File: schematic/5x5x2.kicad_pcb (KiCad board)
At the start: 4 copper layers, 204 x 100 mm, 186 parts, among them J1 SW Debug, J10 Conn_01x03_Female, J11 Conn_01x03_Male, J12 Conn_01x03_Male, J13 Conn_01x03_Female, J14 Conn_01x03_Female, J15 Conn_01x03_Male, J16 Conn_01x03_Female, J2 USB_C_Receptacle_USB2.0, J3 Conn_01x03_Male, J4 Conn_01x03_Male, J5 Conn_01x03_Female, J6 Conn_01x03_Female, J7 Conn_01x03_Male, J8 Conn_01x03_Male, J9 Conn_01x03_Female, SW1 SW, SW11 SW, SW12 SW, SW13 SW, SW14 SW, SW15 SW, SW21 SW, SW22 SW, SW23 SW, SW24 SW, SW25 SW, SW31 SW, SW32 SW, SW33 SW, SW34 SW, SW35 SW, SW41 SW, SW42 SW, SW43 SW, SW44 SW, SW45 SW, SW51 SW, SW52 SW, SW53 SW, SW54 SW, SW55 SW, SW6 ALPS_EC11, U1 SRV0504, U2 STM32F103C8, U3 LD1117S33CTR, Y1 16M

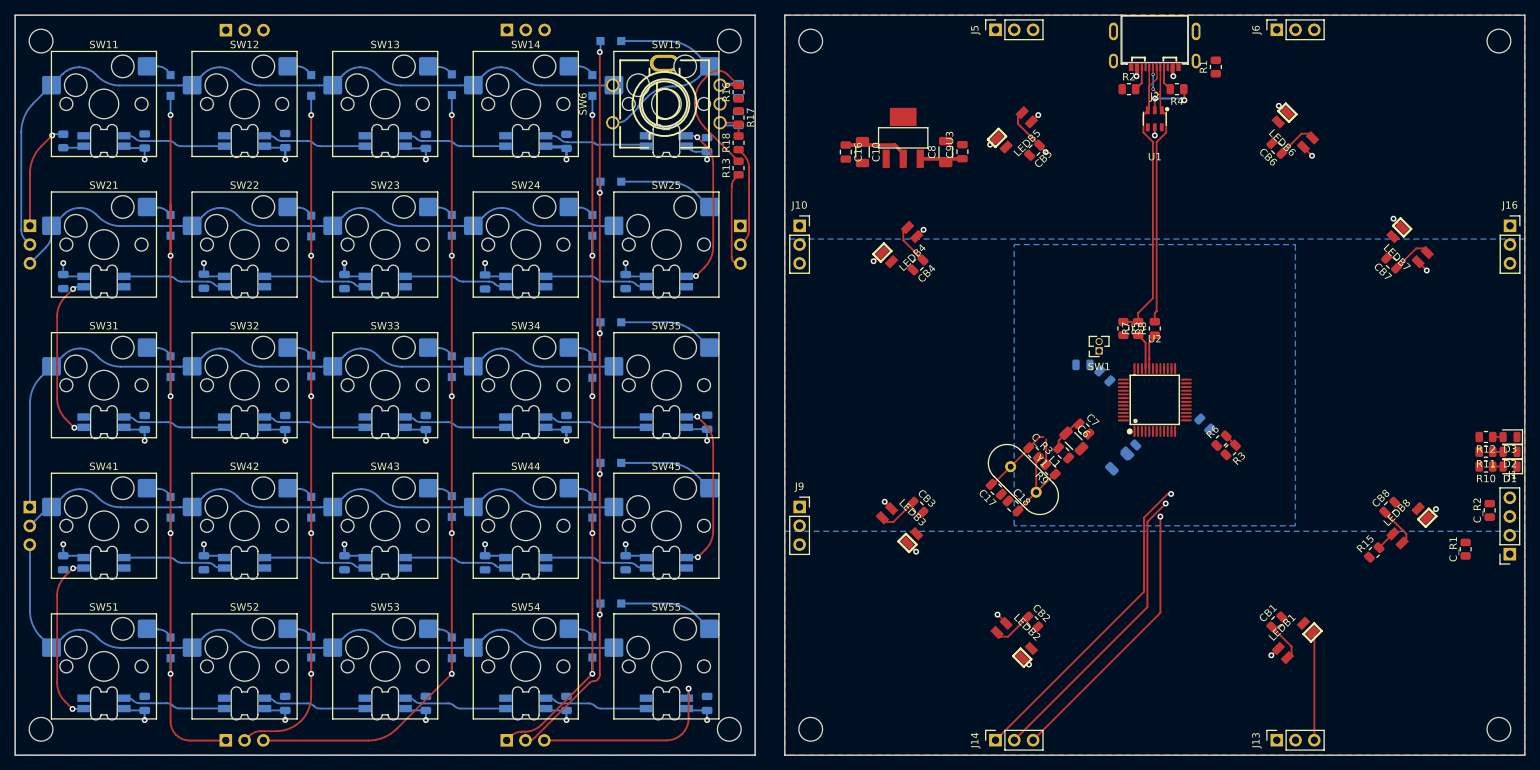
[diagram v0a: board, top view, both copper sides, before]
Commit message: Routed all remaining parts.
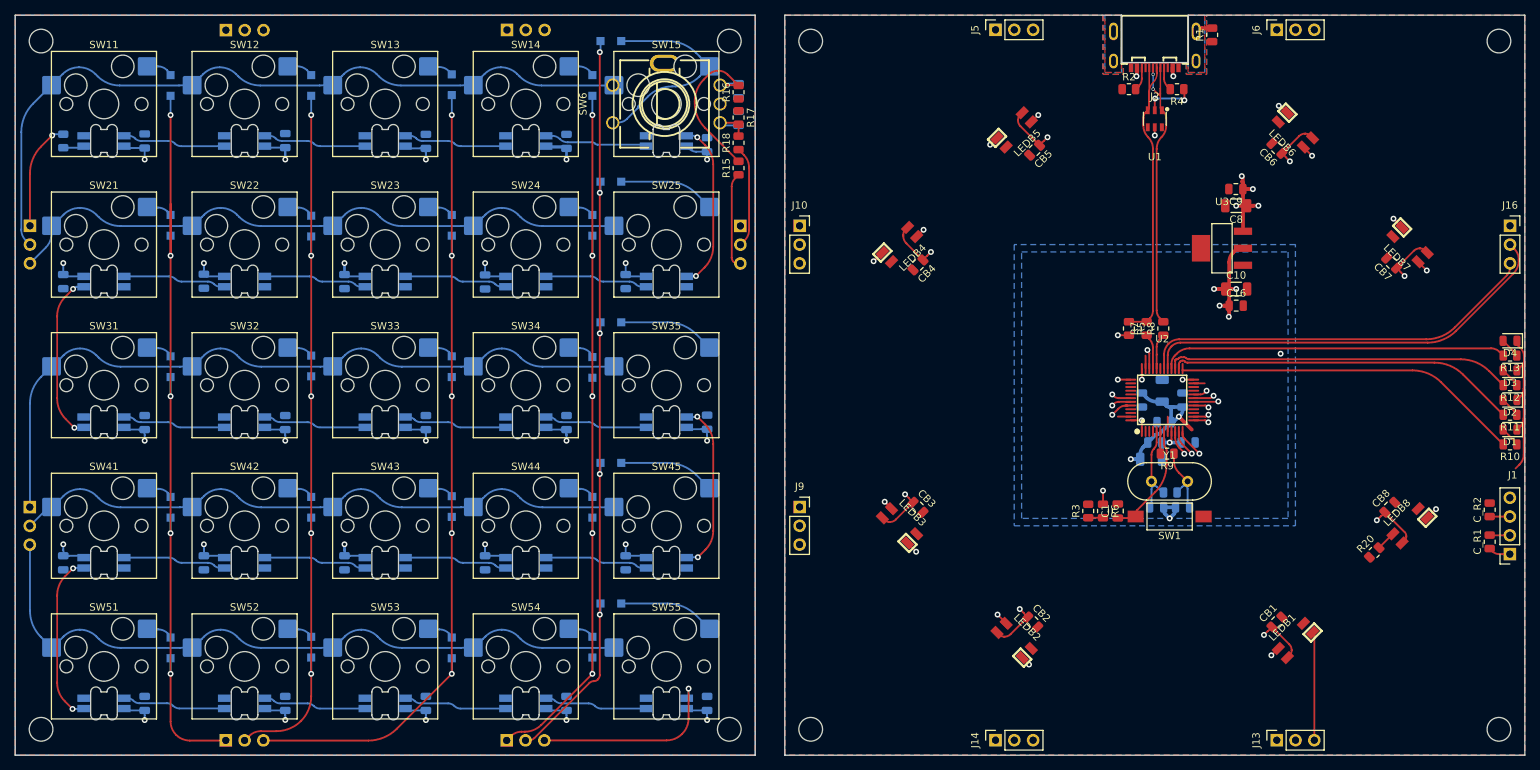
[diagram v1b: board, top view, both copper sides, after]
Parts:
- added D4: Led_Small, LED_SMD:LED_0805_2012Metric, F.Cu at (238.0, 82.0)
- added R13: 1k, Resistor_SMD:R_0805_2012Metric, F.Cu at (238.0, 84.0)
- C1: moved to F.Cu
- C17, C18, C6, C7, C_R3, L1: moved to B.Cu
- SW1: footprint Connector_PinSocket_1.27mm:PinSocket_1x02_P1.27mm_Vertical -> Button_Switch_SMD:SW_SPST_FSMSM
- moved C16 56.7 mm to (201.0, 77.2), turned to 0 degrees
- moved C10 53.8 mm to (201.0, 75.0), turned to 0 degrees
- moved U3 45.6 mm to (199.1, 69.5), turned to 0 degrees
- moved C8 39.9 mm to (201.0, 63.8), turned to 180 degrees
- moved C9 37.3 mm to (200.9, 61.5), turned to 180 degrees
- moved SW1 24.3 mm to (192.0, 105.8)
- moved C18 22.9 mm to (193.8, 104.5), turned to 0 degrees
- moved C17 21.8 mm to (190.2, 104.5), turned to 180 degrees
- moved R3 20.9 mm to (181.0, 105.0), turned to 90 degrees
- moved C1 20.3 mm to (185.0, 105.0), turned to 90 degrees
- moved C_R3 19.3 mm to (192.1, 102.5), turned to 0 degrees
- moved Y1 19.1 mm to (189.6, 101.0), turned to 0 degrees
- moved R6 18.6 mm to (183.0, 105.0), turned to -90 degrees
- moved L1 16.9 mm to (194.5, 95.8), turned to 180 degrees
- moved R9 15.9 mm to (191.7, 97.2), turned to 180 degrees
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- renumbered R13 to R15, R14 to R19, R15 to R20
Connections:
- net /USBD+ renamed Net-(R7-Pad1)
- net /USBD- renamed Net-(R8-Pad1)
- net Net-(C1-Pad1) renamed /~RESET
- net Net-(J2-PadS1) renamed /SHIELD
- U2 pad 2: Net-(R10-Pad2) -> unconnected-(U2-Pad2)
- U2 pad 25: unconnected-(U2-Pad25) -> Net-(R10-Pad2)
- U2 pad 26: unconnected-(U2-Pad26) -> Net-(R11-Pad2)
- U2 pad 27: unconnected-(U2-Pad27) -> Net-(R12-Pad2)
- U2 pad 28: unconnected-(U2-Pad28) -> Net-(U2-Pad28)
- U2 pad 3: Net-(R11-Pad2) -> unconnected-(U2-Pad3)
- U2 pad 4: Net-(R12-Pad2) -> unconnected-(U2-Pad4)
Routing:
- net COL4: track 102.7 -> 179.7 mm, vias 5 -> 6
- net BACKLIGHTIN: track 14.8 -> 88.6 mm, vias 1 -> 2
- net ROW5: track 96.4 -> 166.8 mm, vias 0 -> 1
- net ROTD: track 104.9 -> 175.0 mm, vias 0 -> 1
- net COL5: track 105.6 -> 175.4 mm, vias 5 -> 6
- net Net-(C_R2-Pad1): track 0.00 -> 69.0 mm, vias 0 -> 1
- net ROW2: track 87.7 -> 155.2 mm, vias 0 -> 1
- net ROW4: track 85.5 -> 152.2 mm, vias 0 -> 1
- net Net-(C_R1-Pad2): track 0.00 -> 64.6 mm, vias 0 -> 1
- net ROW3: track 101.5 -> 161.8 mm, vias 0 -> 1
- net +3V3: track 8.96 -> 67.7 mm, vias 0 -> 9
- net GND: track 7.20 -> 65.0 mm, vias 2 -> 5
- net ROTA: track 13.7 -> 71.3 mm
- net ROTB: track 13.1 -> 67.5 mm
- net Net-(R11-Pad2): track 0.00 -> 47.4 mm
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- added copper zone on B.Cu, net /SHIELD
- added copper zone on F.Cu, net /SHIELD

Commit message: Cleaned up silkscreen.
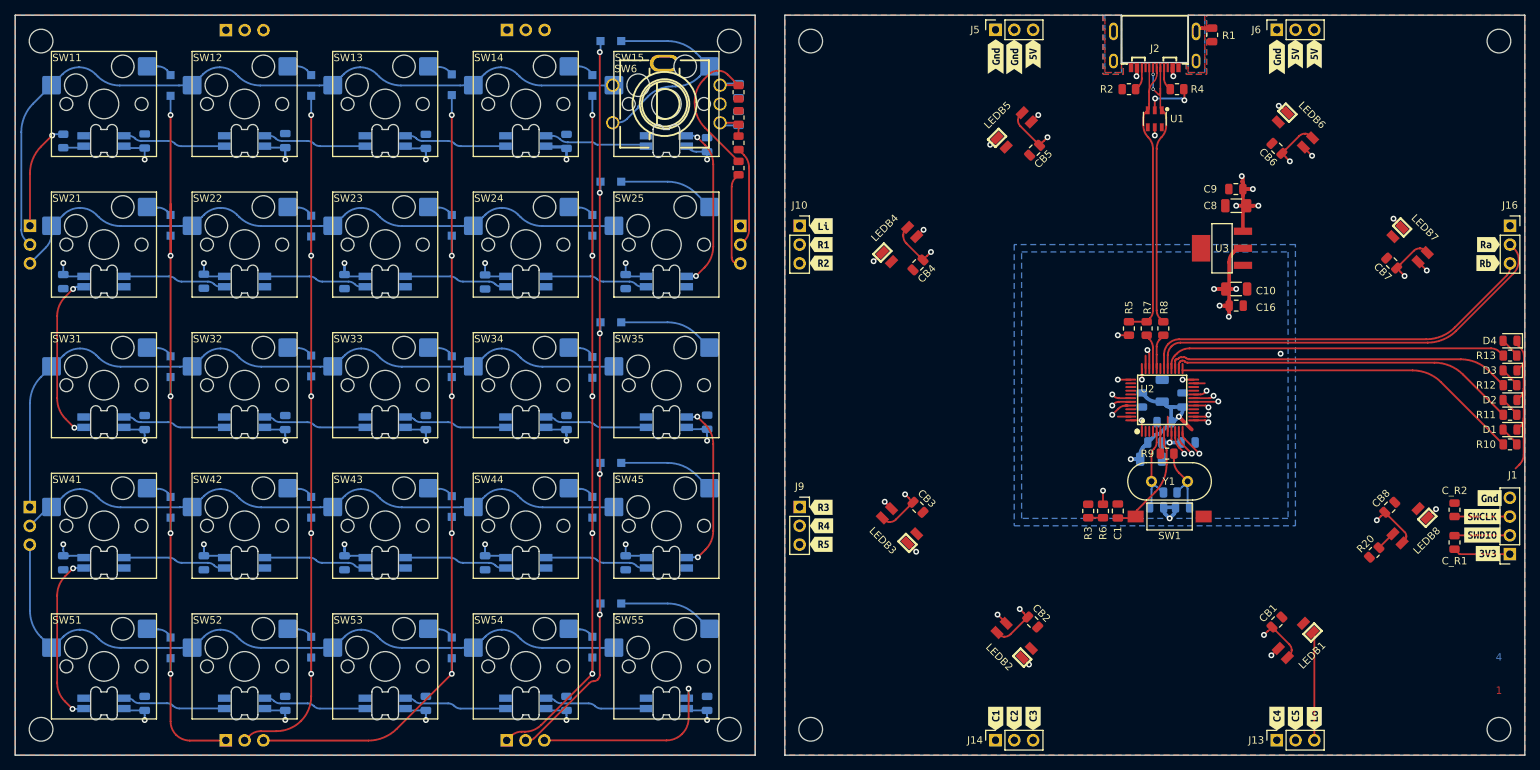
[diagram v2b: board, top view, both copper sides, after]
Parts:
- added G***: LOGO, LOGO, B.Cu at (131.2, 112.8)
- added G***: LOGO, LOGO, B.Cu at (190.0, 133.8)
- added kibuzzard-62AF6B0E: G***, kibuzzard-62AF6B0E, B.Cu at (38.0, 102.0)
- added kibuzzard-62AF6B38: G***, kibuzzard-62AF6B38, B.Cu at (40.5, 107.0)
- added kibuzzard-62AF6B38: G***, kibuzzard-62AF6B38, B.Cu at (145.0, 107.0)
- added kibuzzard-62AF6B7C: G***, kibuzzard-62AF6B7C, B.Cu at (145.0, 109.5)
- added kibuzzard-62AF6B7C: G***, kibuzzard-62AF6B7C, B.Cu at (40.5, 109.5)
- added kibuzzard-62AF6BA3: G***, kibuzzard-62AF6BA3, B.Cu at (145.0, 71.5)
- added kibuzzard-62AF6BA3: G***, kibuzzard-62AF6BA3, B.Cu at (40.5, 71.5)
- added kibuzzard-62AF6BAD: G***, kibuzzard-62AF6BAD, B.Cu at (40.5, 69.0)
- added kibuzzard-62AF6BAD: G***, kibuzzard-62AF6BAD, B.Cu at (145.0, 69.0)
- added kibuzzard-62AF6BF3: G***, kibuzzard-62AF6BF3, B.Cu at (38.0, 63.8)
- added kibuzzard-62AF6D1E: G***, kibuzzard-62AF6D1E, B.Cu at (72.5, 40.0)
- added kibuzzard-62AF6D1E: G***, kibuzzard-62AF6D1E, B.Cu at (110.5, 40.0)
- added kibuzzard-62AF6DB1: G***, kibuzzard-62AF6DB1, B.Cu at (99.0, 40.0)
- added kibuzzard-62AF6DB1: G***, kibuzzard-62AF6DB1, B.Cu at (61.0, 40.0)
- added kibuzzard-62AF6E15: G***, kibuzzard-62AF6E15, B.Cu at (131.5, 69.0)
- added kibuzzard-62AF6E21: G***, kibuzzard-62AF6E21, B.Cu at (131.5, 71.5)
- added kibuzzard-62AF6EB6: G***, kibuzzard-62AF6EB6, B.Cu at (99.8, 136.0)
- added kibuzzard-62AF6EDD: G***, kibuzzard-62AF6EDD, B.Cu at (62.0, 136.0)
- added kibuzzard-62AF6F00: G***, kibuzzard-62AF6F00, B.Cu at (72.2, 136.0)
- added kibuzzard-62AF6F11: G***, kibuzzard-62AF6F11, B.Cu at (110.0, 136.0)
- added kibuzzard-62AF73B1: G***, kibuzzard-62AF73B1, F.Cu at (171.0, 43.6)
- added kibuzzard-62AF73B1: G***, kibuzzard-62AF73B1, F.Cu at (206.5, 43.6)
- added kibuzzard-62AF73B1: G***, kibuzzard-62AF73B1, F.Cu at (168.5, 43.6)
- added kibuzzard-62AF73B1: G***, kibuzzard-62AF73B1, B.Cu at (168.5, 43.8)
- added kibuzzard-62AF73B1: G***, kibuzzard-62AF73B1, B.Cu at (206.5, 43.8)
- added kibuzzard-62AF73B1: G***, kibuzzard-62AF73B1, B.Cu at (171.0, 43.8)
- added kibuzzard-62AF73D1: G***, kibuzzard-62AF73D1, F.Cu at (211.6, 43.2)
- added kibuzzard-62AF73D1: G***, kibuzzard-62AF73D1, F.Cu at (209.0, 43.2)
- added kibuzzard-62AF73D1: G***, kibuzzard-62AF73D1, F.Cu at (173.6, 43.2)
- added kibuzzard-62AF73D1: G***, kibuzzard-62AF73D1, B.Cu at (209.0, 43.2)
- added kibuzzard-62AF73D1: G***, kibuzzard-62AF73D1, B.Cu at (211.5, 43.2)
- added kibuzzard-62AF73D1: G***, kibuzzard-62AF73D1, B.Cu at (173.5, 43.2)
- added kibuzzard-62AF7423: G***, kibuzzard-62AF7423, F.Cu at (235.1, 69.0)
- added kibuzzard-62AF7423: G***, kibuzzard-62AF7423, B.Cu at (243.2, 66.0)
- added kibuzzard-62AF742E: G***, kibuzzard-62AF742E, F.Cu at (235.1, 71.5)
- added kibuzzard-62AF742E: G***, kibuzzard-62AF742E, B.Cu at (243.2, 68.5)
- added kibuzzard-62AF7487: G***, kibuzzard-62AF7487, F.Cu at (206.5, 133.1)
- added kibuzzard-62AF7487: G***, kibuzzard-62AF7487, B.Cu at (206.5, 133.0)
- added kibuzzard-62AF7492: G***, kibuzzard-62AF7492, F.Cu at (209.0, 133.1)
- added kibuzzard-62AF7492: G***, kibuzzard-62AF7492, B.Cu at (209.0, 133.0)
- added kibuzzard-62AF749F: G***, kibuzzard-62AF749F, F.Cu at (211.6, 133.1)
- added kibuzzard-62AF749F: G***, kibuzzard-62AF749F, B.Cu at (211.5, 133.0)
- added kibuzzard-62AF74B5: G***, kibuzzard-62AF74B5, F.Cu at (168.5, 133.1)
- added kibuzzard-62AF74B5: G***, kibuzzard-62AF74B5, B.Cu at (168.5, 133.0)
- added kibuzzard-62AF74BF: G***, kibuzzard-62AF74BF, F.Cu at (171.0, 133.1)
- added kibuzzard-62AF74BF: G***, kibuzzard-62AF74BF, B.Cu at (171.0, 133.0)
- added kibuzzard-62AF74C8: G***, kibuzzard-62AF74C8, F.Cu at (173.6, 133.1)
- added kibuzzard-62AF74C8: G***, kibuzzard-62AF74C8, B.Cu at (173.5, 133.0)
- added kibuzzard-62AF74DA: G***, kibuzzard-62AF74DA, F.Cu at (144.9, 104.5)
- added kibuzzard-62AF74E3: G***, kibuzzard-62AF74E3, F.Cu at (144.9, 107.0)
- added kibuzzard-62AF74EC: G***, kibuzzard-62AF74EC, F.Cu at (144.9, 109.5)
- added kibuzzard-62AF74F7: G***, kibuzzard-62AF74F7, F.Cu at (144.9, 71.5)
- added kibuzzard-62AF74FE: G***, kibuzzard-62AF74FE, F.Cu at (144.9, 69.0)
- added kibuzzard-62AF750A: G***, kibuzzard-62AF750A, F.Cu at (144.9, 66.5)
- added kibuzzard-62AF7A14: G***, kibuzzard-62AF7A14, F.Cu at (235.2, 103.2)
- added kibuzzard-62AF7A14: G***, kibuzzard-62AF7A14, B.Cu at (235.2, 103.2)
- added kibuzzard-62AF7A28: G***, kibuzzard-62AF7A28, F.Cu at (234.2, 105.8)
- added kibuzzard-62AF7A28: G***, kibuzzard-62AF7A28, B.Cu at (234.2, 105.8)
- added kibuzzard-62AF7A49: G***, kibuzzard-62AF7A49, F.Cu at (234.2, 108.2)
- added kibuzzard-62AF7A49: G***, kibuzzard-62AF7A49, B.Cu at (234.2, 108.2)
- added kibuzzard-62AF7A56: G***, kibuzzard-62AF7A56, F.Cu at (235.0, 110.8)
- added kibuzzard-62AF7A56: G***, kibuzzard-62AF7A56, B.Cu at (235.0, 110.8)
- added kibuzzard-62AF7CA9: G***, kibuzzard-62AF7CA9, B.Cu at (145.0, 104.5)
- added kibuzzard-62AF7CCF: G***, kibuzzard-62AF7CCF, B.Cu at (145.0, 66.5)
- moved C_R1 4.75 mm to (230.5, 109.2)
- moved C_R2 4.75 mm to (230.5, 104.8)
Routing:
- net +3V3: track 67.7 -> 72.4 mm
- net Net-(C_R1-Pad2): track 64.6 -> 69.4 mm
- net Net-(C_R2-Pad1): track 69.0 -> 73.5 mm
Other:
- board text added: "1"
- board text added: "2"
- board text added: "202206"
- board text added: "3"
- board text added: "4"
- board text added: "JLCJLCJLCJLC"
